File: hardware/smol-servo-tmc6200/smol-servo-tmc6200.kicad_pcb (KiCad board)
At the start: 4 copper layers, 48 x 44.5 mm, 121 parts, among them J1 Conn_01x05, J2 C31-S-RA-CS1A-BK-SS, J3 TC-2050, J4 Screw_Terminal_01x02, J5 Screw_Terminal_01x02, J7 Conn_01x03, J8 Conn_01x03, J9 Conn_01x02, M1 Motor_2_or_3_phase, Q1 NVTFS5C658NL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

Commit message: rearrange TMC6200 version to have MCU closer to driver chip
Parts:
- added R50: 1K, Resistor_SMD:R_0402_1005Metric, F.Cu at (152.4, 103.6)
- moved L1 32.2 mm to (169.0, 120.9)
- moved J2 31.7 mm to (171.0, 114.0), turned to 90 degrees
- moved R28 31.2 mm to (166.1, 122.8), turned to 90 degrees
- moved D4 30.6 mm to (167.1, 122.8)
- moved R29 30.6 mm to (168.1, 122.8)
- moved J1 25.6 mm to (155.1, 100.3), turned to -90 degrees
- moved R3 25.2 mm to (142.9, 102.6), turned to 0 degrees
- moved R2 22.2 mm to (146.7, 102.6), turned to 0 degrees
- moved R22 22.0 mm to (144.8, 102.6), turned to 180 degrees
- moved F1 21.8 mm to (162.0, 121.3), turned to 90 degrees
- moved J9 21.2 mm to (161.4, 100.3), turned to -90 degrees
- moved D1 21.1 mm to (162.0, 112.8)
- moved R4 19.0 mm to (162.0, 115.3), turned to 90 degrees
- moved R1 18.9 mm to (150.5, 102.6)
- moved R21 18.7 mm to (148.6, 102.6), turned to 180 degrees
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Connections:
- J9 pad 2: SYNC -> Net-(J9-Pad2)
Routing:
- net SDA3: track 26.3 -> 3.80 mm, vias 2 -> 0
- net SYNC: track 22.7 -> 3.32 mm, vias 2 -> 0
- net MOSI: track 46.4 -> 27.0 mm, vias 2 -> 4
- net MISO: track 48.0 -> 28.8 mm
- net SLCK: track 43.9 -> 26.9 mm, vias 2 -> 3
- net DRVSEL: track 38.4 -> 25.5 mm, vias 4 -> 2
- net ENA: track 29.7 -> 17.8 mm
- net ASEL: track 30.9 -> 19.9 mm, vias 0 -> 2
- net DRVEN: track 31.5 -> 21.3 mm
- net VBUS: track 46.6 -> 36.7 mm
- net VDD: track 107.3 -> 97.5 mm, vias 9 -> 8
- net DM: track 26.4 -> 17.2 mm, vias 3 -> 2
- net DP: track 23.9 -> 15.0 mm
- net ENC: track 35.0 -> 26.2 mm
- net SWCLK: track 4.04 -> 12.7 mm, vias 0 -> 2
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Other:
- board text added: "GND SYNC"
- board text added: "GND VDD 3V3 ENCI ENCA ENCB"
- board text added: "RX"
- board text added: "SMOL-SERVO-TMC6200 V0.6.0 (c) 2022-08 dgulyas@inrobco.de"
- board text added: "STM32G4"
- board text added: "TMC6200"
- board text added: "TX"
- board text removed: "ENCB ENCA ENCI 3V3 VDD GND"
- board text removed: "I2C:SCL-SDA"
- board text removed: "SMOL-SERVO-TMC6200 V0.5.0 (c) 2022-07 dgulyas@inrobco.de"
- board text removed: "UART:TX-RX"

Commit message: v0.6.0 PCB order
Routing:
- net GND: track 96.0 -> 94.3 mm, vias 76 -> 75
- net PWMR: track 15.1 -> 14.5 mm

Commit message: v0.6.1 hardware
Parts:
- C22: footprint Capacitor_SMD:C_0402_1005Metric -> Capacitor_SMD:C_0603_1608Metric
- moved C22 0.75 mm to (132.2, 127.1)
- moved C26 0.72 mm to (133.2, 127.8)
- moved R37 0.64 mm to (134.9, 129.9)
- moved C27 0.64 mm to (134.0, 129.0)
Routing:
- net VDD: track 97.5 -> 96.2 mm
- net Net-(C22-Pad2): track 2.69 -> 3.67 mm
- net Net-(C26-Pad2): track 1.46 -> 2.01 mm
- net Net-(C26-Pad1): track 5.81 -> 6.33 mm
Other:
- board text added: "SMOL-SERVO-TMC6200 V0.6.1 (c) 2022-08 dgulyas@inrobco.de"
- board text removed: "SMOL-SERVO-TMC6200 V0.6.0 (c) 2022-08 dgulyas@inrobco.de"

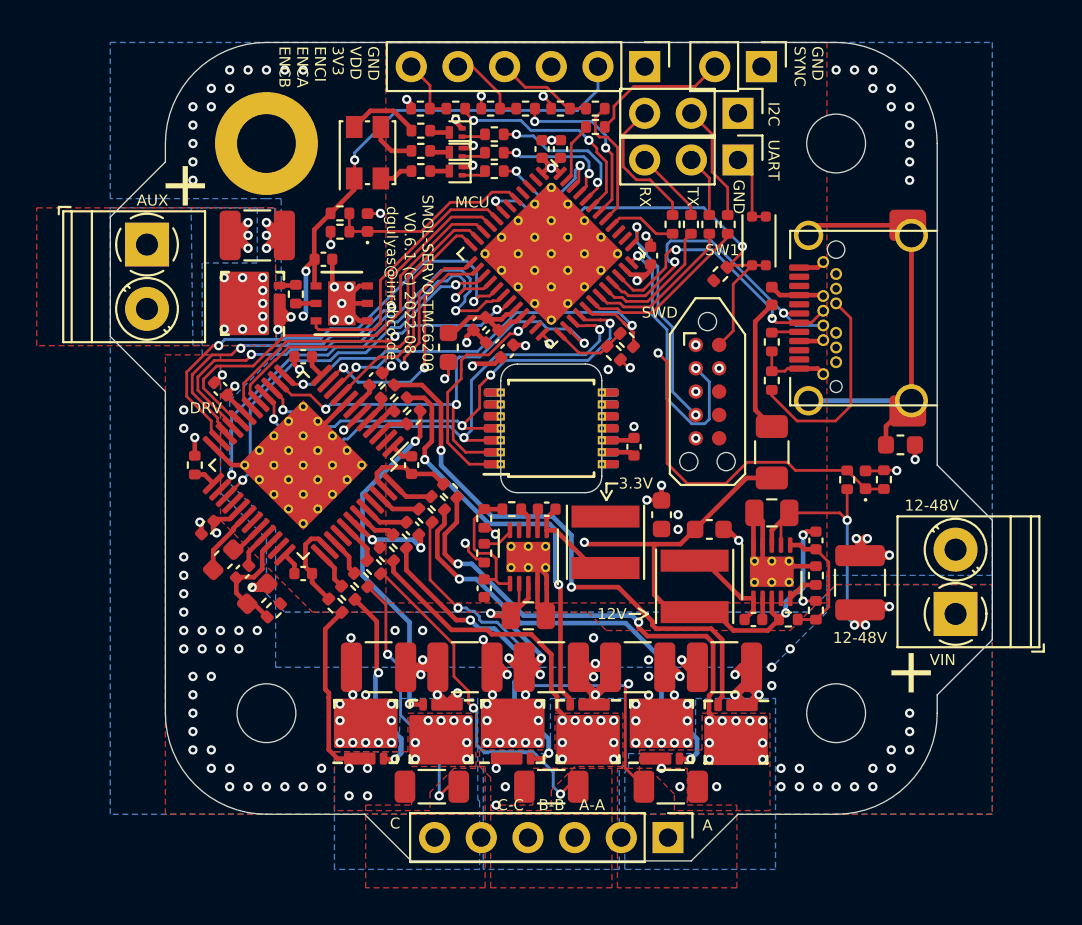
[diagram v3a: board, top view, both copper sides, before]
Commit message: add v0.7.0 prelim hardware design with USB Power Delivery
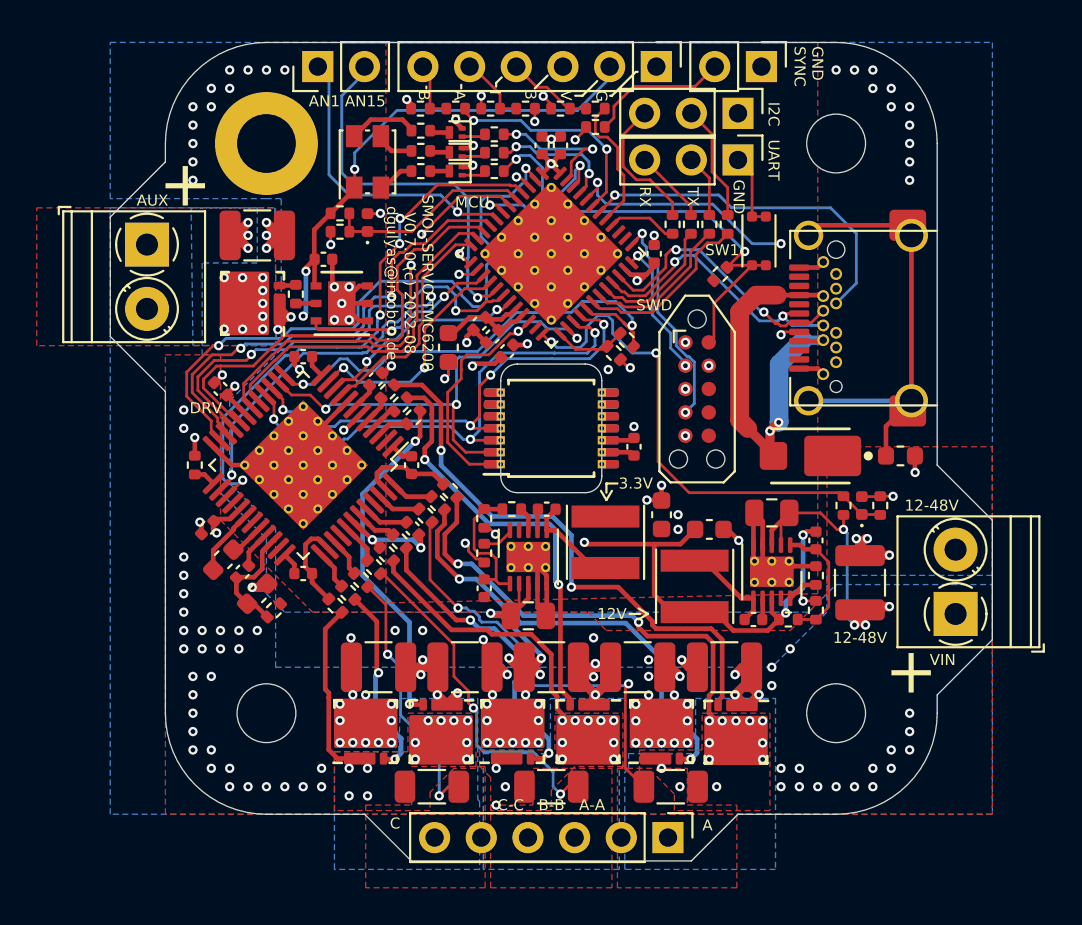
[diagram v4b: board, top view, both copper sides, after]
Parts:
- removed F1: 500mA, Fuse:Fuse_1206_3216Metric
- removed R4, R5: 5K1, Resistor_SMD:R_0402_1005Metric
- added J6: Conn_01x02, Connector_PinHeader_2.54mm:PinHeader_1x02_P2.54mm_Vertical, F.Cu at (137.3, 100.3)
- D1: value 1A -> 5A 50V; footprint Diode_SMD:D_0402_1005Metric -> stm32-nema17:Diode-SMPA-DO-221BC
- moved D1 8.95 mm to (164.1, 121.5), turned to 180 degrees
- moved R29 1.42 mm to (167.9, 124.2)
- moved D4 1.41 mm to (166.9, 124.2)
- moved R28 1.41 mm to (165.9, 124.2)
- moved J1 0.63 mm to (155.7, 100.3)
- moved L1 0.60 mm to (169.0, 121.5)
- moved J3 0.58 mm to (157.9, 117.9)
- moved D3 0.50 mm to (140.0, 105.5)
- moved C3 0.22 mm to (155.6, 110.5)
- moved C1 0.20 mm to (149.5, 104.6)
- moved C4 0.20 mm to (150.5, 104.6)
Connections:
- D1 pad 1: Net-(D1-Pad1) -> VBUS
- J2 pad A5: Net-(J2-PadA5) -> USB_CC1
- J2 pad B5: Net-(J2-PadB5) -> USB_CC2
- U1 pad 13: SOB -> SYNC
- U1 pad 14: SOC -> ENCA
- U1 pad 15: DRVEN -> PWMR
- U1 pad 16: DRVFAULT -> SOC
- U1 pad 17: ENC -> ADC1_15
- U1 pad 19: ENA -> SOB
- U1 pad 2: unconnected-(U1-Pad2) -> ENC
- U1 pad 3: unconnected-(U1-Pad3) -> ENA
- U1 pad 4: unconnected-(U1-Pad4) -> DRVEN
- U1 pad 42: ENCA -> USB_CC2
- U1 pad 44: LEDB -> USB_CC1
- U1 pad 47: SYNC -> LEDB
- U1 pad 6: unconnected-(U1-Pad6) -> DRVFAULT
- U1 pad 8: PWMR -> ADC1_1
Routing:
- net ADC1_15: track 0.00 -> 20.7 mm, vias 0 -> 1
- net USB_CC1: track 0.00 -> 20.4 mm, vias 0 -> 3
- net USB_CC2: track 0.00 -> 19.6 mm, vias 0 -> 1
- net Net-(D1-Pad2): track 7.49 -> 26.3 mm, vias 0 -> 2
- net ADC1_1: track 0.00 -> 16.3 mm, vias 0 -> 1
- net Net-(J2-PadB5): track 11.4 -> 0.00 mm
- net DRVEN: track 21.3 -> 30.5 mm, vias 2 -> 4
- net ENC: track 26.2 -> 34.8 mm
- net ENA: track 17.8 -> 25.9 mm
- net SYNC: track 3.32 -> 11.2 mm, vias 0 -> 2
- net SWDIO: track 15.0 -> 7.59 mm
- net Net-(D1-Pad1): track 7.36 -> 0.00 mm
- net VDD: track 96.2 -> 91.2 mm
- net PWMR: track 14.5 -> 10.6 mm, vias 0 -> 2
- net DRVFAULT: track 23.6 -> 27.5 mm, vias 2 -> 3
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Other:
- board text added: "AN1 AN15"
- board text added: "G V 3 I A B"
- board text added: "SMOL-SERVO-TMC6200 V0.7.0 (c) 2022-08 dgulyas@inrobco.de"
- board text removed: "GND VDD 3V3 ENCI ENCA ENCB"
- board text removed: "SMOL-SERVO-TMC6200 V0.6.1 (c) 2022-08 dgulyas@inrobco.de"
